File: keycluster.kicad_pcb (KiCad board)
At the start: 2 copper layers, 45.1 x 52.6 mm, 63 parts, among them P2 CONN_5, P7 CONN_10, P9 CONN_5, SW1 CT05-3050-G1, U1 MKL03Z32VFK4, U2 IS31FL3737, U4 ESD

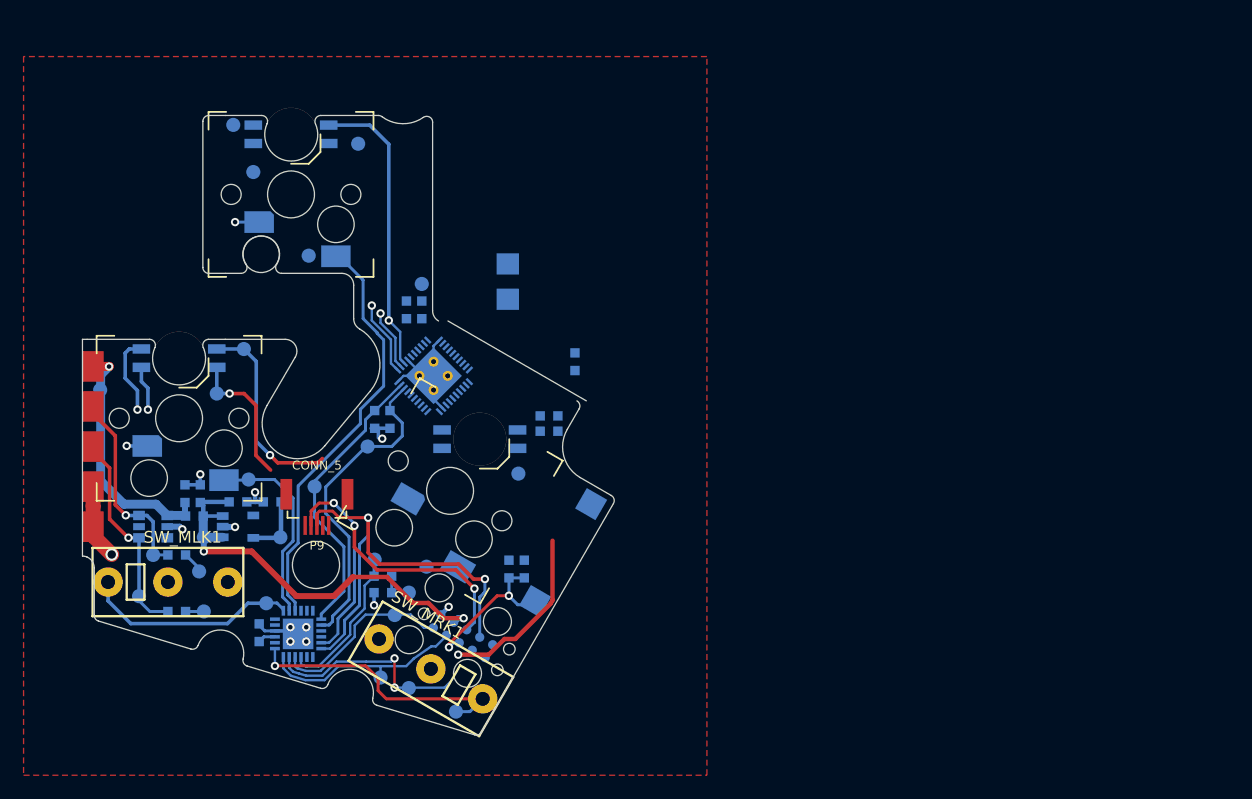
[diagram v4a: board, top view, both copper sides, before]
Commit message: Wiring on main pcb and 7pin FFC added.
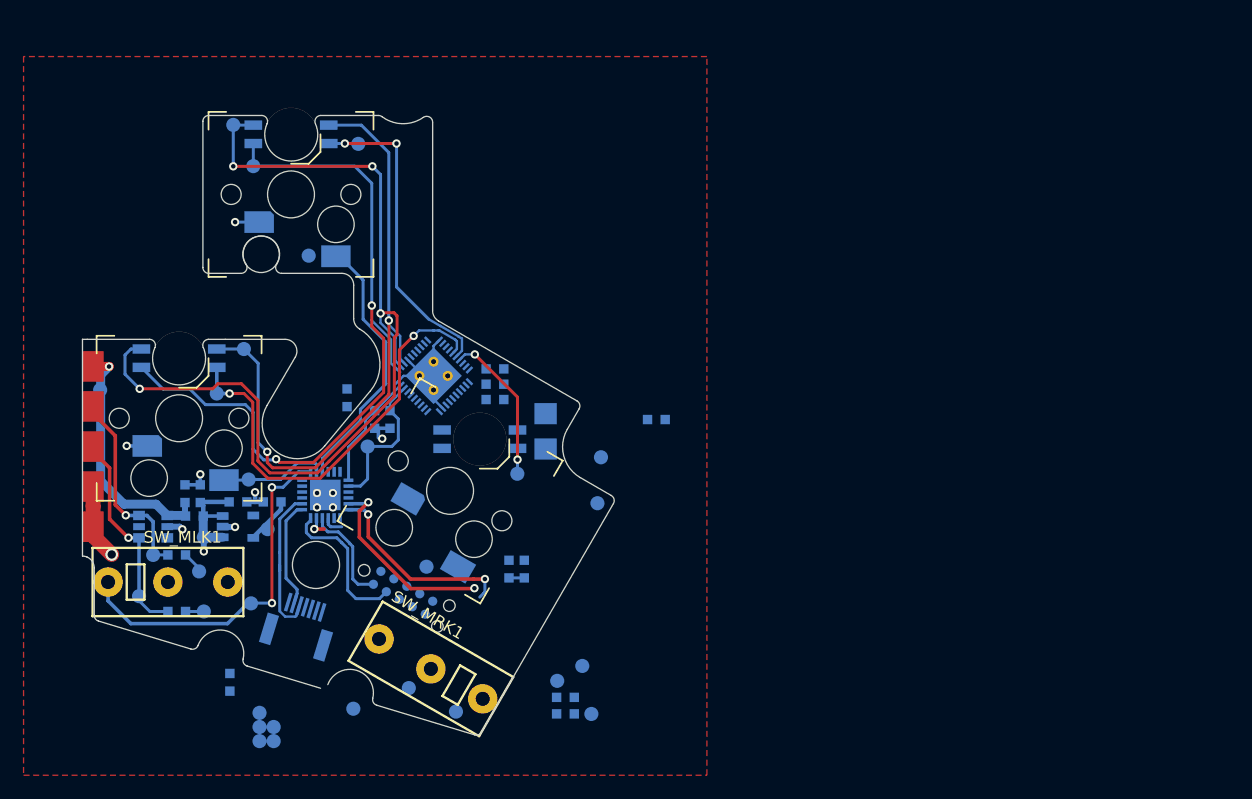
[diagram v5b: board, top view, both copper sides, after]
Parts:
- removed P9: CONN_5, FFC_Connector_51281-0594
- removed SW1: CT05-3050-G1, UGL:Reed_Switch_CT05-3050-G1
- added P8: CONN_7, UGL:FFC_Connector_51281-0794, B.Cu at (142.7, 126.8)
- added TP_TB_BTN1: TB_BTN1, UGL:Test_Point, B.Cu at (140.0, 131.7)
- added TP_TB_DOWN1: TB_DOWN1, UGL:Test_Point, B.Cu at (141.2, 132.9)
- added TP_TB_LEFT1: TB_LEFT1, UGL:Test_Point, B.Cu at (141.2, 134.1)
- added TP_TB_RIGHT1: TB_RIGHT1, UGL:Test_Point, B.Cu at (140.0, 132.9)
- added TP_TB_UP1: TB_UP1, UGL:Test_Point, B.Cu at (140.0, 134.1)
- P7: footprint UGL:Tag_Connect_2x5_Header_With_Legs -> UGL:Tag_Connect_2x5_Header_With_No_Legs
- TP_KEY_LEFT1: value KEYS_ROW2 -> KEY_LEFT1
- TP_KEY_MLEFT1: value KEYS_ROW4 -> KEY_MLEFT1
- TP_KEY_MRIGHT1: value KEYS_ROW5 -> KEY_MRIGHT1
- TP_KEY_RIGHT1: value KEYS_ROW3 -> KEY_RIGHT1
- TP_KEY_TOP1: value KEYS_ROW1 -> KEYS_TOP1
- moved TP_IICRST1 24.4 mm to (169.0, 110.0)
- moved TP_CS1 24.4 mm to (136.4, 104.6)
- moved TP_CS2 24.4 mm to (148.4, 83.4)
- moved TP_GND1 23.8 mm to (168.7, 113.9)
- moved R8 19.6 mm to (147.5, 105.0), turned to 270 degrees
- moved TP_TEST_LED_R1 18.6 mm to (168.2, 131.8)
- moved D2 18.6 mm to (166.0, 131.8)
- moved R2 18.6 mm to (166.0, 130.4)
- moved TP_TEST_LED1 18.6 mm to (165.3, 129.0)
- moved TP_SWDCLK1 16.5 mm to (167.4, 127.7)
- moved C13 13.1 mm to (164.3, 107.8), turned to 270 degrees
- moved U1 12.0 mm to (145.6, 113.2)
- moved C15 9.82 mm to (160.0, 105.1), turned to 0 degrees
- moved C19 9.16 mm to (173.7, 106.8)
- moved C17 9.03 mm to (160.0, 102.5), turned to 0 degrees
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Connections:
- D_LK1 pad 4: /LED_CS2 -> /LED_CS1
- D_TK1 pad 4: /LED_CS1 -> /LED_CS2
- U1 pad 1: /KEY_MRIGHT -> /TB_BTN
- U1 pad 11: Net-(U1-Pad11) -> /KEY_MRIGHT
- U1 pad 15: Net-(U1-Pad15) -> /TB_LEFT
- U1 pad 2: Net-(U1-Pad2) -> /TB_RIGHT
- U1 pad 5: Net-(U1-Pad5) -> /TB_UP
- U1 pad 6: Net-(U1-Pad6) -> /TB_DOWN
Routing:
- net /LED_SW2: track 11.9 -> 79.0 mm, vias 2 -> 4
- net /LED_SW1: track 10.2 -> 65.6 mm
- net /LED_CS1: track 0.00 -> 37.6 mm, vias 0 -> 2
- net /RESET: track 31.8 -> 3.16 mm, vias 4 -> 1
- net +5V: track 36.6 -> 9.84 mm, vias 2 -> 1
- net /KEY_MRIGHT: track 23.6 -> 0.00 mm, vias 1 -> 0
- net /ADDR: track 40.7 -> 18.8 mm
- net +3V3: track 23.3 -> 4.03 mm, vias 1 -> 0
- net /SCL: track 36.3 -> 18.1 mm, vias 3 -> 2
- net /LED_CS2: track 12.0 -> 27.9 mm, vias 1 -> 2
- net /IICRST: track 24.8 -> 10.0 mm
- net /LED_SW3: track 42.0 -> 56.6 mm
- net /SDB: track 27.2 -> 12.8 mm
- net /LED_CS3: track 0.00 -> 14.2 mm, vias 0 -> 2
- net /TB_RIGHT: track 0.00 -> 13.2 mm
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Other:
- outline, holes or cut-outs redrawn

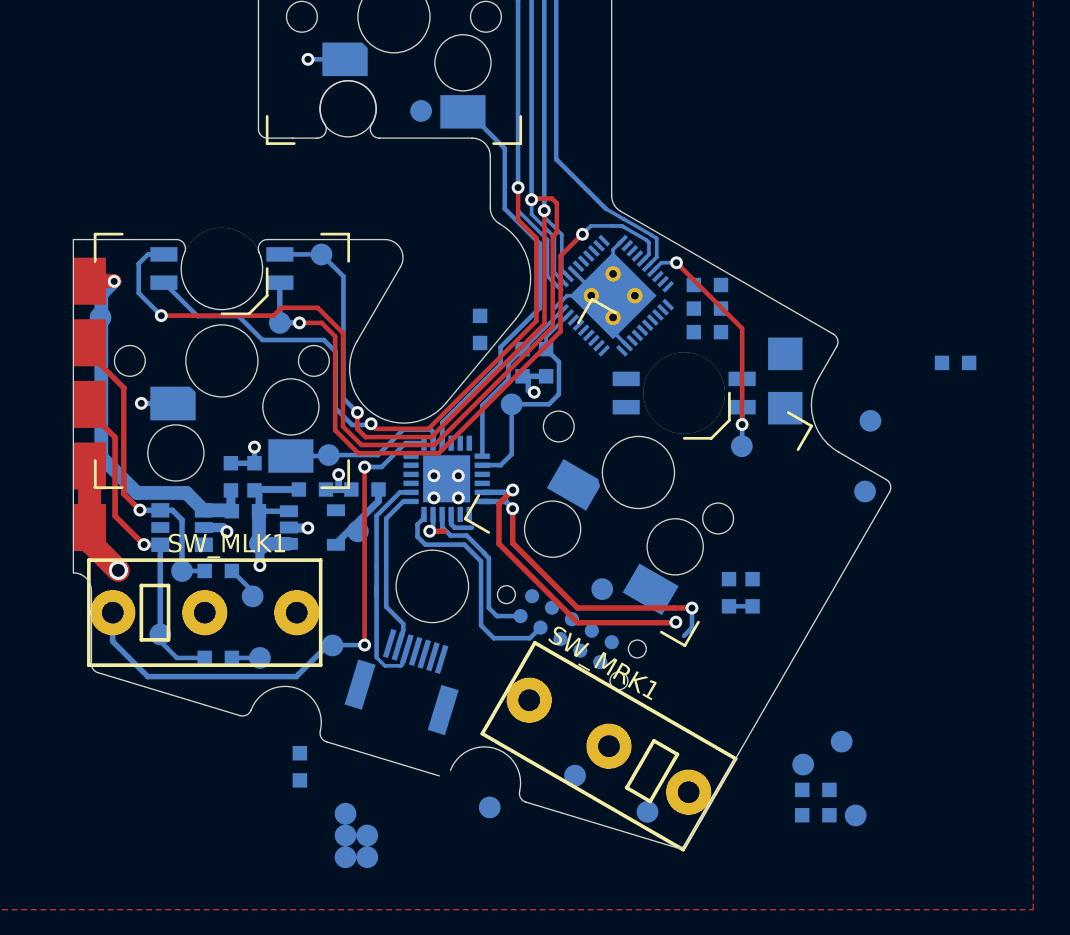
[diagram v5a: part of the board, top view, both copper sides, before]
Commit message: Wiring on main pcb.
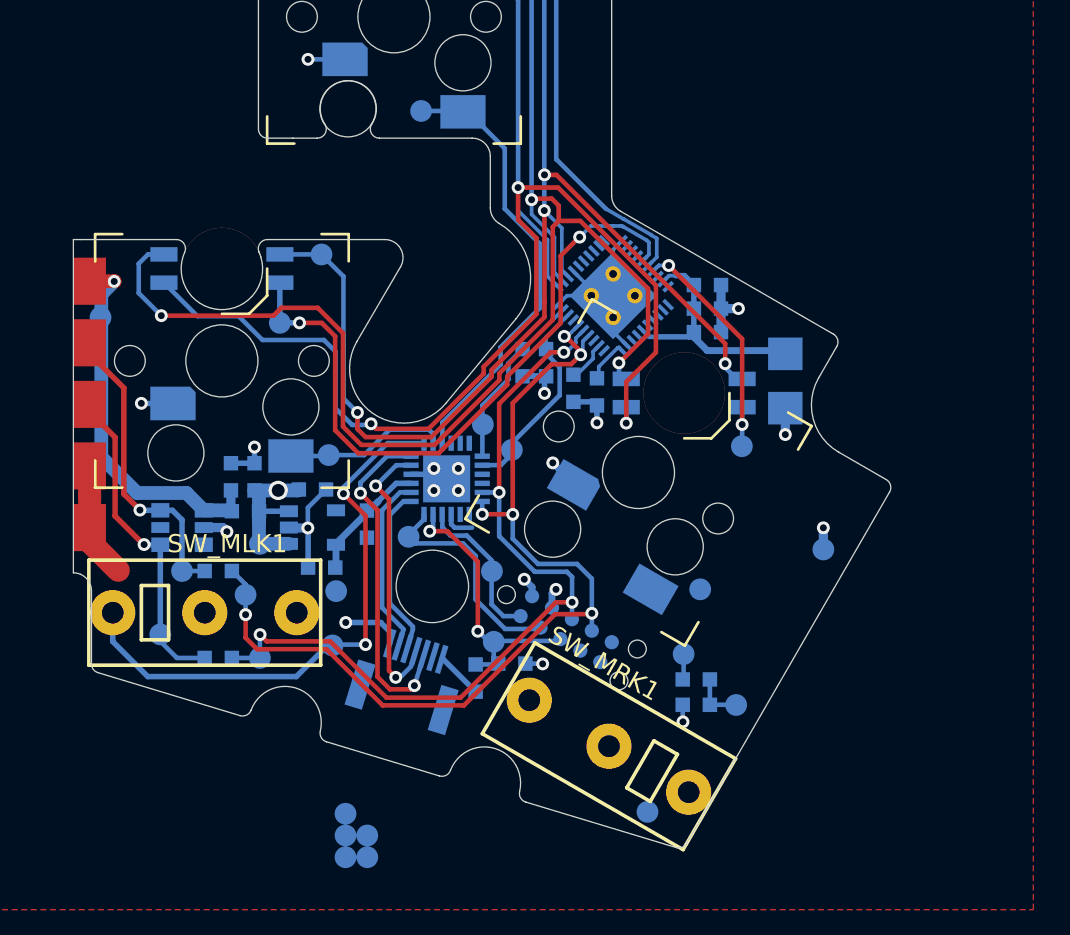
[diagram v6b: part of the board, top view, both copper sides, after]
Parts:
- moved TP_SWDCLK1 21.5 mm to (148.1, 118.3)
- moved TP_IICRST1 21.4 mm to (147.6, 110.2)
- moved C19 21.1 mm to (152.6, 108.2), turned to 270 degrees
- moved TP_SWDIO1 15.6 mm to (143.5, 116.4)
- moved R1 14.8 mm to (147.2, 124.2), turned to 90 degrees
- moved C3 13.9 mm to (149.2, 123.4), turned to 180 degrees
- moved C12 11.1 mm to (138.7, 118.1), turned to 0 degrees
- moved TP_TEST_LED1 8.99 mm to (158.7, 122.9)
- moved D2 8.99 mm to (159.4, 125.7)
- moved TP_TEST_LED_R1 8.99 mm to (161.6, 125.7)
- moved R2 8.99 mm to (159.4, 124.3)
- moved TP_RESET1 8.65 mm to (148.2, 122.2)
- moved R8 7.32 mm to (153.9, 108.4)
- moved TP_KEY_RIGHT1 5.41 mm to (159.6, 119.3)
- moved TP_GND1 3.94 mm to (166.4, 117.1)
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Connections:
- P8 pad 2: /TB_UP -> /TB_LEFT
- P8 pad 4: /TB_LEFT -> /TB_UP
- U1 pad 1: /TB_BTN -> /TB_RIGHT
- U1 pad 2: /TB_RIGHT -> /TB_BTN
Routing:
- net /ADDR: track 18.8 -> 53.5 mm, vias 2 -> 6
- net /SCL: track 18.1 -> 45.6 mm, vias 2 -> 4
- net GND: track 26.8 -> 47.6 mm, vias 12 -> 19
- net /LED_SW1: track 65.6 -> 84.6 mm, vias 2 -> 3
- net /TB_DOWN: track 0.00 -> 18.7 mm, vias 0 -> 2
- net /LED_SW3: track 56.6 -> 73.0 mm, vias 2 -> 4
- net /TB_UP: track 0.00 -> 15.5 mm, vias 0 -> 2
- net +5V: track 9.84 -> 24.6 mm, vias 1 -> 2
- net /LED_SW2: track 79.0 -> 91.6 mm, vias 4 -> 5
- net /RESET: track 3.16 -> 15.7 mm, vias 1 -> 2
- net +3V3: track 4.03 -> 11.7 mm
- net /TB_RIGHT: track 13.2 -> 9.24 mm
- net /TEST_LED_R: track 0.00 -> 2.85 mm
- net /R_EXT: track 0.00 -> 2.47 mm
- net /KEY_TOP: track 22.5 -> 24.8 mm
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
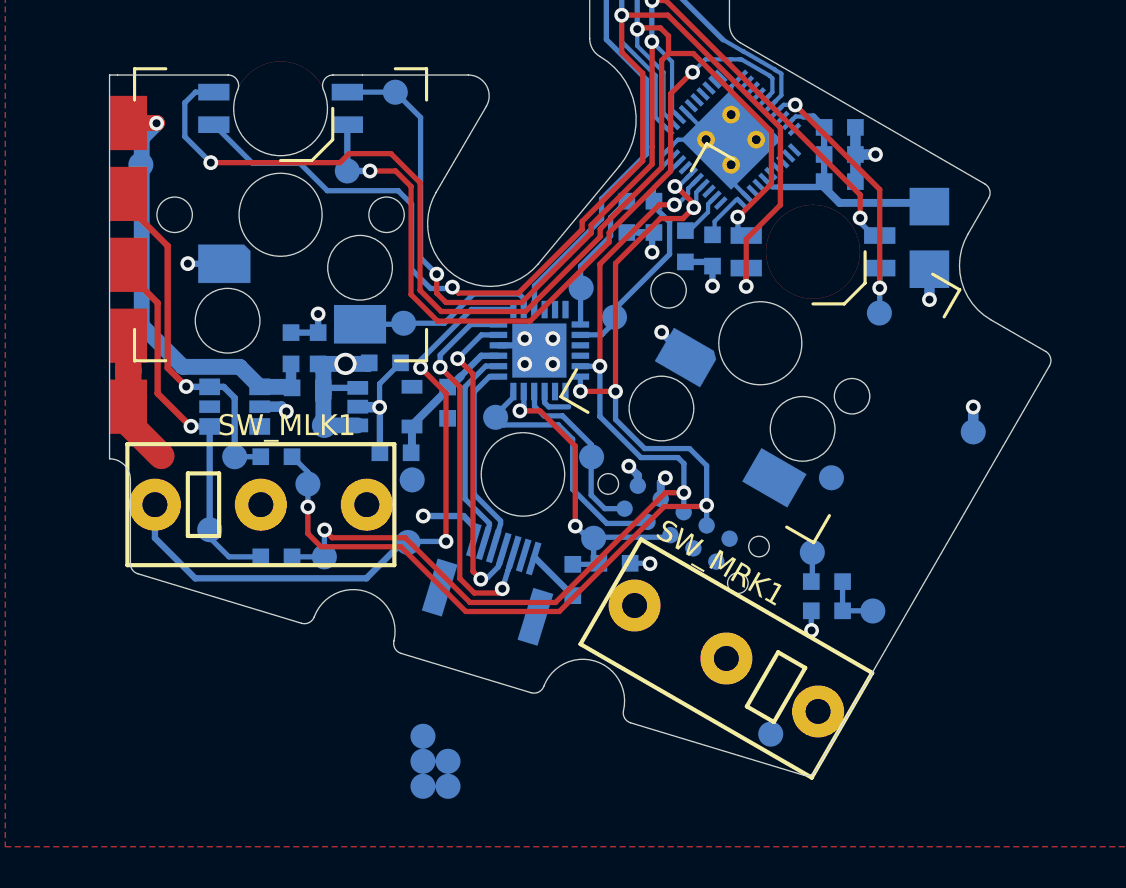
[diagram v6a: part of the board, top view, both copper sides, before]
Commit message: Wiring on main pcb.
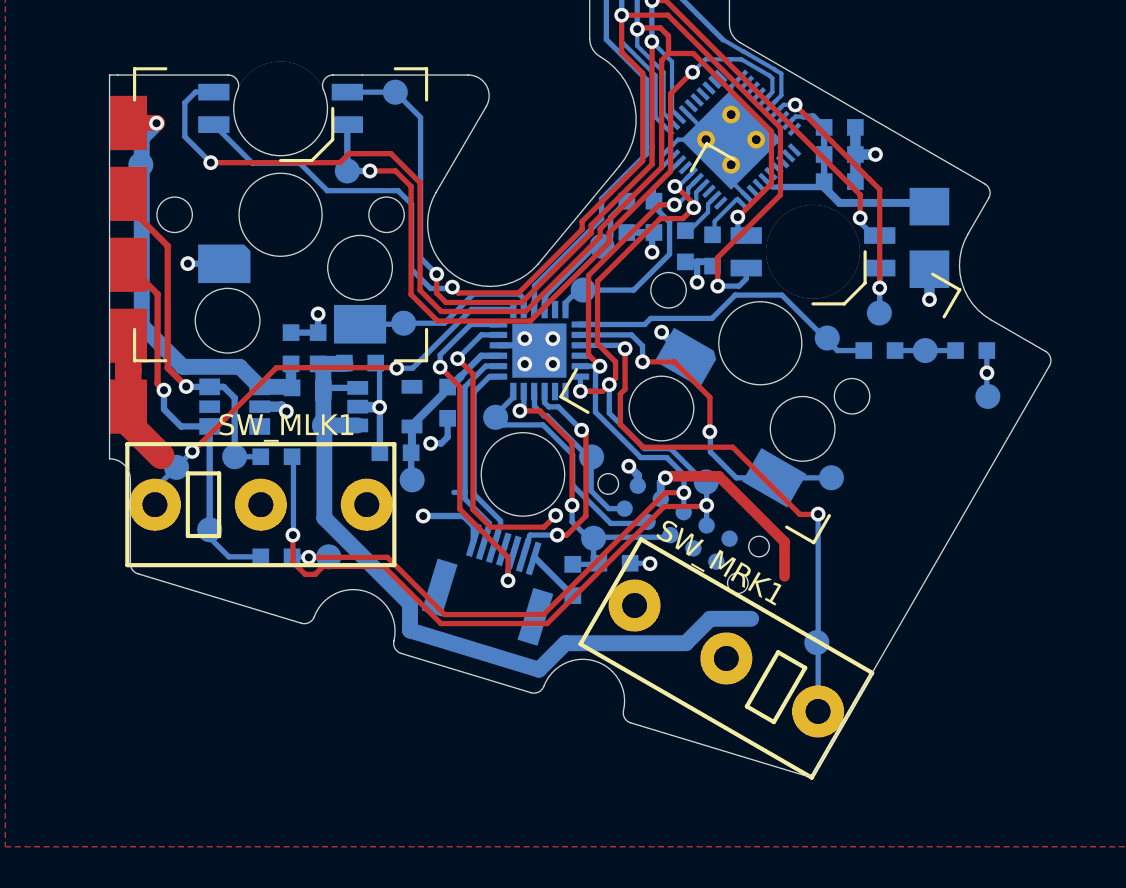
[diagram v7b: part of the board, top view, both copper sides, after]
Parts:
- removed TP_TB_BTN1: TB_BTN1, UGL:Test_Point
- removed TP_TB_DOWN1: TB_DOWN1, UGL:Test_Point
- removed TP_TB_LEFT1: TB_LEFT1, UGL:Test_Point
- removed TP_TB_RIGHT1: TB_RIGHT1, UGL:Test_Point
- removed TP_TB_UP1: TB_UP1, UGL:Test_Point
- moved TP_SDA1 19.1 mm to (153.6, 119.5)
- moved D2 14.3 mm to (166.3, 113.2), turned to 180 degrees
- moved TP_TEST_LED_R1 12.7 mm to (164.1, 113.2)
- moved TP_KEY_MLEFT1 11.7 mm to (128.2, 118.8)
- moved R2 11.4 mm to (161.9, 113.2)
- moved TP_TEST_LED1 10.3 mm to (159.4, 112.6)
- moved TP_KEY_MRIGHT1 4.91 mm to (158.9, 127.2)
- moved TP_IICRST1 2.24 mm to (148.6, 108.2)
- moved TP_SDB1 1.98 mm to (147.7, 110.3)
- moved TP_GND1 1.84 mm to (167.1, 115.4)
- moved C2 1.19 mm to (137.0, 113.8)
- moved TP_SCL1 0.21 mm to (135.5, 123.1)
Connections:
- U1 pad 10: /KEY_RIGHT -> /IICRST
- U1 pad 11: /KEY_MRIGHT -> Net-(U1-Pad11)
- U1 pad 12: Net-(U1-Pad12) -> /SDB
- U1 pad 13: /IICRST -> /TEST_LED
- U1 pad 14: /SDB -> /KEY_RIGHT
- U1 pad 15: /TB_LEFT -> /KEY_MRIGHT
- U1 pad 21: /TEST_LED -> /TB_LEFT
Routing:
- net +5V: track 24.6 -> 61.3 mm, vias 2 -> 1
- net /KEY_MRIGHT: track 0.00 -> 26.7 mm, vias 0 -> 2
- net /KEY_RIGHT: track 0.00 -> 17.0 mm, vias 0 -> 2
- net /TEST_LED: track 3.17 -> 15.3 mm
- net /TB_LEFT: track 0.00 -> 11.0 mm, vias 0 -> 2
- net /KEY_MLEFT: track 31.6 -> 21.5 mm
- net /ADDR: track 53.5 -> 56.1 mm
- net GND: track 47.6 -> 49.9 mm
- net /TB_DOWN: track 18.7 -> 17.0 mm
- net /LED_SW1: track 84.6 -> 86.3 mm
- net /IICRST: track 10.0 -> 11.5 mm
- net +3V3: track 11.7 -> 13.0 mm
- net /TB_UP: track 15.5 -> 14.5 mm
- net /SWDIO: track 12.7 -> 12.2 mm
- net /SWDCLK: track 8.50 -> 7.95 mm
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
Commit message: First final version pcb of main board.
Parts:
- TP_CS1: value LED_CS1 -> LCS1
- TP_CS2: value LED_CS2 -> LCS2
- TP_CS3: value LED_CS3 -> LCS3
- TP_IICRST1: value IICRST -> IRST
- TP_KEY_LEFT1: value KEY_LEFT1 -> KL
- TP_KEY_MLEFT1: value KEY_MLEFT1 -> KML
- TP_KEY_MRIGHT1: value KEY_MRIGHT1 -> KMR
- TP_KEY_RIGHT1: value KEY_RIGHT1 -> KR
- TP_KEY_TOP1: value KEYS_TOP1 -> KT
- TP_RESET1: value RESET -> RST
- TP_SCL_BOTTOM1: value SCL_BOTTOM -> SCL_B
- TP_SDA_BOTTOM1: value SDA_BOTTOM -> SDA_B
- TP_SW1: value LED_SW1 -> LSW1
- TP_SW2: value LED_SW2 -> LSW2
- TP_SW3: value LED_SW3 -> LSW3
- TP_TEST_LED1: value TEST_LED -> TL
- TP_TEST_LED_R1: value TEST_LED_R -> TLR
- TP_VCC_BOTTOM1: value VCC_BOTTOM -> VCC_B
- moved R30 4.71 mm to (149.2, 111.1), turned to 180 degrees
- moved C17 2.76 mm to (161.9, 104.5), turned to 90 degrees
- moved TP_SDB1 2.53 mm to (150.1, 109.5)
- moved R3 1.49 mm to (148.8, 107.9)
- moved C19 1.22 mm to (151.4, 108.0)
- moved TP_IICRST1 1.21 mm to (147.5, 108.7)
- moved TP_KEY_MRIGHT1 1.10 mm to (158.9, 128.3)
- moved TP_SDA1 0.50 mm to (153.6, 119.0)
- moved TP_CS3 0.40 mm to (162.3, 111.4)
- moved P7 0.30 mm to (152.2, 121.2)
- moved C16 0.20 mm to (160.0, 104.0)
- moved R8 0.20 mm to (153.9, 108.6)
- moved C15 0.20 mm to (160.0, 105.3)
- moved TP_SWDCLK1 0.20 mm to (148.1, 118.1)
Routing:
- net +3V3: track 13.0 -> 73.0 mm, vias 0 -> 5
- net +5V: track 61.3 -> 96.4 mm, vias 1 -> 6
- net /TB_UP: track 14.5 -> 17.5 mm
- net GND: track 49.9 -> 47.9 mm, vias 19 -> 21
- net /SDB: track 11.5 -> 10.8 mm
- net /LED_CS3: track 13.7 -> 14.4 mm
- net /LED_SW1: track 86.3 -> 86.8 mm
- net /ADDR: track 56.1 -> 56.7 mm
- net /TB_BTN: track 10.5 -> 9.99 mm
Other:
- board text added: "UHK 60 Key cluster v0.1.0"
